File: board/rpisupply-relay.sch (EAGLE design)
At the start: 23 parts, among them IC1 ATTINY45-20SU, K1 5V, SW1 SCHURTER-LSH-1301.x, T1 BC107, X1 MINI-USB, X2 AVR-ISP-6-EDGE

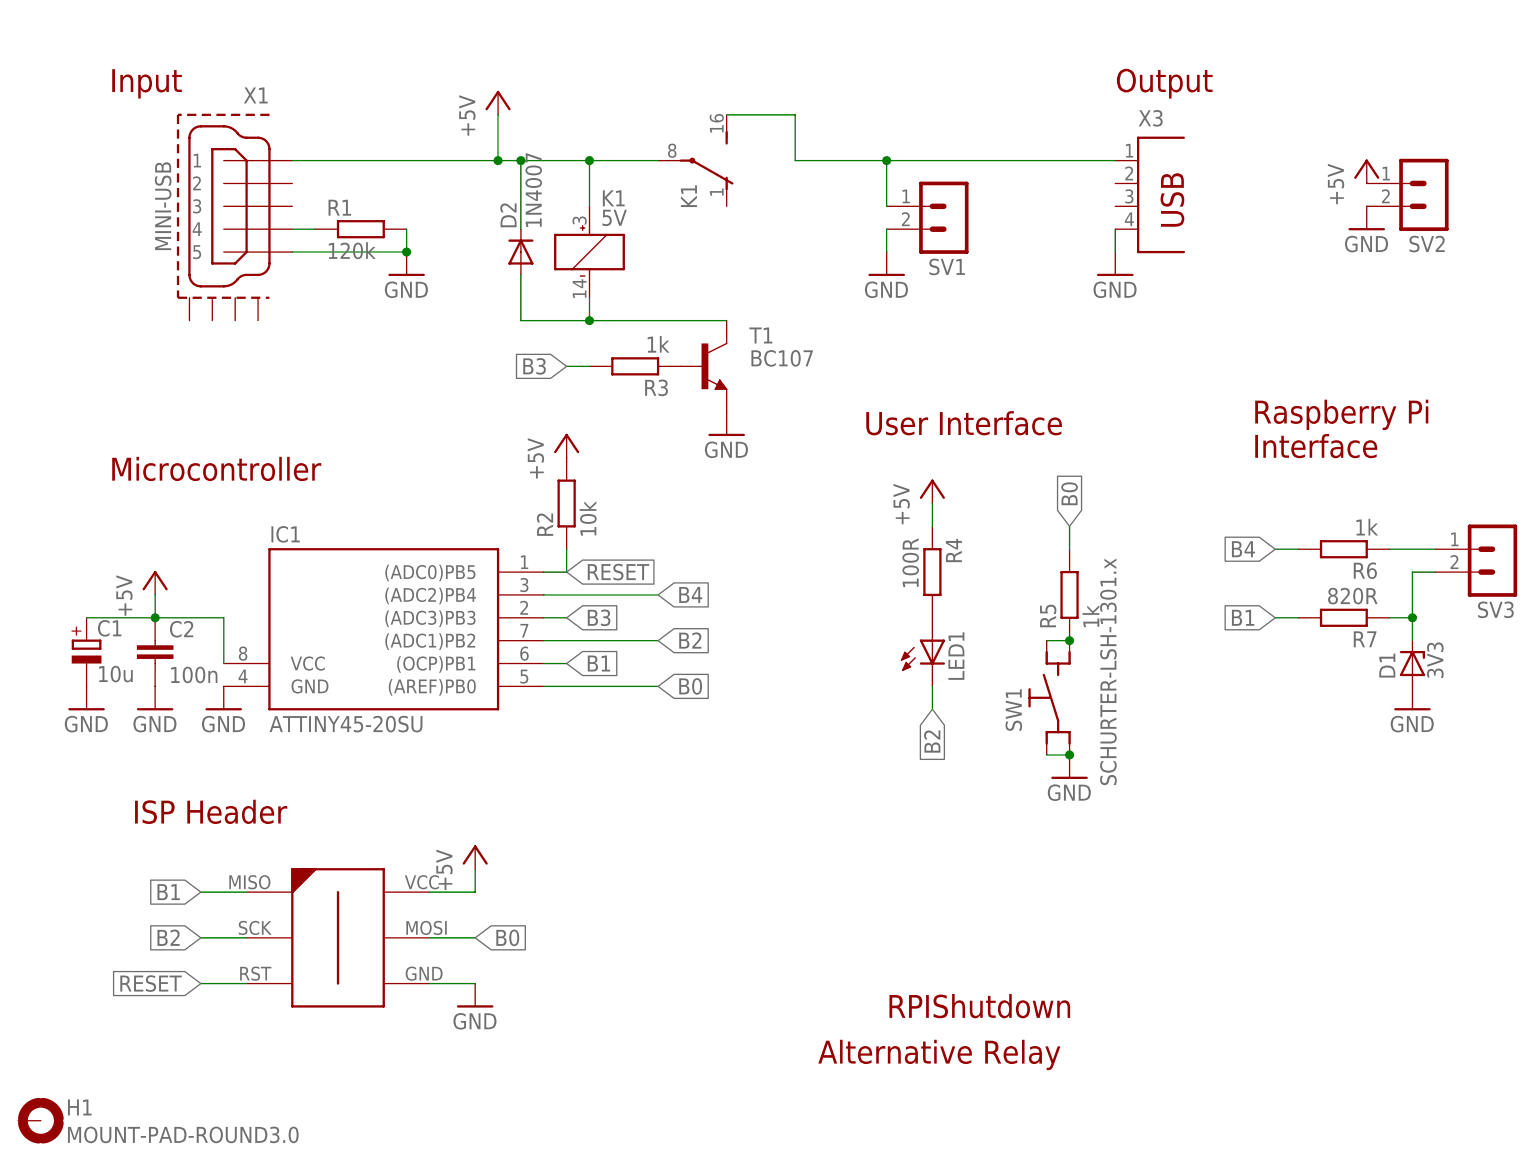
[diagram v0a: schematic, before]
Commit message: add images for documentation
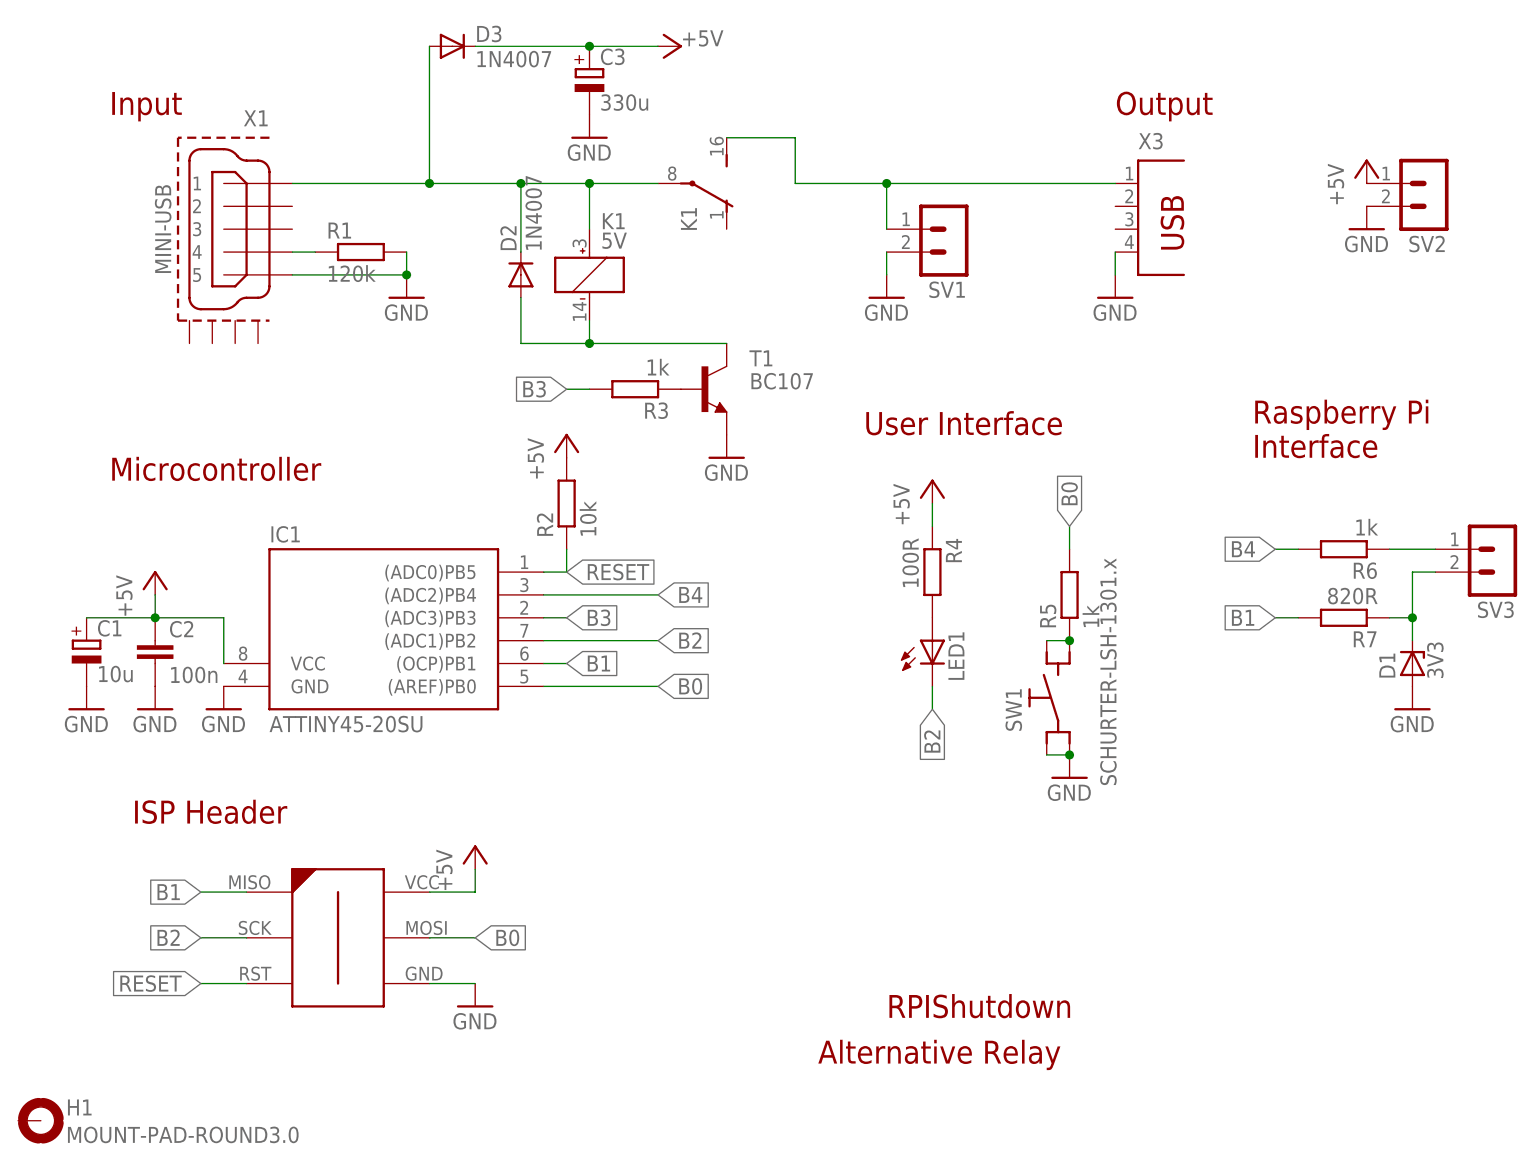
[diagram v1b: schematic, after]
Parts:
- added C3: 330u, rcl:CPOL-EUSMCC
- added D3: 1N4007, diode:1N4004
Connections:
- new net N$8: D2.C, D3.A, K1-1.+, K1-2.P, X1.1
- net +5V: now also C3.+, D3.C; no longer D2.C, K1-1.+, K1-2.P, X1.1
- net B3: now also R3.2
- net GND: now also C3.-
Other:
- moved on the sheet: D2, K1, R1, R3, SV1, T1, X1, X3

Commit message: Change frame in schematics
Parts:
- removed D1: 3V3, diode:ZENER-DIODESOD80C
- added R8: 1k8, rcl:R-EU_R0805
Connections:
- net GND: now also R8.2; no longer D1.A
- net N$2: now also R8.1; no longer D1.C
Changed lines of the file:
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@@
 <?xml version="1.0" encoding="utf-8"?>
 <!DOCTYPE eagle SYSTEM "eagle.dtd">
-<eagle version="6.6.0">
+<eagle version="7.4.0">
 <drawing>
 <settings>
@@
 <part name="R6" library="rcl" deviceset="R-EU_" device="R0805" value="1k"/>
 <part name="R7" library="rcl" deviceset="R-EU_" device="R0805" value="820R"/>
-<part name="D1" library="diode" deviceset="ZENER-DIODE" device="SOD80C" value="3V3"/>
 <part name="SV3" library="con-lstb" deviceset="MA02-1R" device=""/>
 <part name="GND2" library="supply1" deviceset="GND" device=""/>
@@
 <part name="D3" library="diode" deviceset="1N4004" device="" value="1N4007"/>
 <part name="GND12" library="supply1" deviceset="GND" device=""/>
+<part name="R8" library="rcl" deviceset="R-EU_" device="R0805" value="1k8"/>
 </parts>
 <sheets>
@@
 <instance part="R6" gate="G$1" x="152.4" y="68.58" rot="R180"/>
 <instance part="R7" gate="G$1" x="152.4" y="60.96" rot="R180"/>
-<instance part="D1" gate="G$1" x="160.02" y="55.88" rot="R90"/>
 <instance part="SV3" gate="G$1" x="170.18" y="68.58" rot="R180"/>
-<instance part="GND2" gate="1" x="160.02" y="50.8"/>
+<instance part="GND2" gate="1" x="160.02" y="45.72"/>
 <instance part="P+2" gate="1" x="66.04" y="81.28"/>
 <instance part="SV1" gate="G$1" x="109.22" y="104.14" rot="R180"/>
@@
 <instance part="X3" gate="G$1" x="129.54" y="104.14"/>
 <instance part="GND5" gate="1" x="48.26" y="96.52"/>
-<instance part="R1" gate="G$1" x="43.18" y="101.6"/>
+<instance part="R1" gate="G$1" x="43.18" y="101.6" smashed="yes">
+<attribute name="NAME" x="39.37" y="103.0986" size="1.778" layer="95"/>
+<attribute name="VALUE" x="44.704" y="103.124" size="1.778" layer="96"/>
+</instance>
 <instance part="GND7" gate="1" x="127" y="96.52"/>
 <instance part="H1" gate="G$1" x="7.62" y="5.08"/>
@@
 <instance part="D3" gate="1" x="53.34" y="124.46"/>
 <instance part="GND12" gate="1" x="68.58" y="114.3"/>
+<instance part="R8" gate="G$1" x="160.02" y="53.34" rot="R270"/>
 </instances>
 <busses>
@@
 <pinref part="IC1" gate="G$1" pin="GND"/>
 <pinref part="GND1" gate="1" pin="GND"/>
-</segment>
-<segment>
-<pinref part="D1" gate="G$1" pin="A"/>
-<pinref part="GND2" gate="1" pin="GND"/>
 </segment>
 <segment>
@@
 <pinref part="C3" gate="G$1" pin="-"/>
 <pinref part="GND12" gate="1" pin="GND"/>
+</segment>
+<segment>
+<pinref part="R8" gate="G$1" pin="2"/>
+<pinref part="GND2" gate="1" pin="GND"/>
 </segment>
 </net>
@@
 <pinref part="SV3" gate="G$1" pin="2"/>
 <wire x1="162.56" y1="66.04" x2="160.02" y2="66.04" width="0.1524" layer="91"/>
-<pinref part="D1" gate="G$1" pin="C"/>
 <wire x1="160.02" y1="66.04" x2="160.02" y2="60.96" width="0.1524" layer="91"/>
 <pinref part="R7" gate="G$1" pin="1"/>
@@
 <wire x1="157.48" y1="60.96" x2="160.02" y2="60.96" width="0.1524" layer="91"/>
 <junction x="160.02" y="60.96"/>
+<pinref part="R8" gate="G$1" pin="1"/>
 </segment>
 </net>
